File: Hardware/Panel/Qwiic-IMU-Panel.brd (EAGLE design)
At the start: 101.6 x 102.6 mm, 288 parts, among them J10 PTH, J11 SMD, J12 SPI, J17 SMD, J18 PTH, J19 SMD, J2 SMD, J20 SPI, J25 SMD, J26 PTH, J27 SMD, J28 SPI, J3 PTH, J33 SMD, J34 PTH, J35 SMD, J36 SPI, J4 SMD, J41 SMD, J42 PTH, J43 SMD, J44 SPI, J49 SMD, J50 PTH, J51 SMD, J52 SPI, J57 SMD, J58 PTH, J59 SMD, J6 SPI, J60 SPI, J65 SMD, J66 PTH, J67 SMD, J68 SPI, J9 SMD, U1 BNO080, U2 BNO080, U3 BNO080, U4 BNO080, U5 BNO080, U6 BNO080, U7 BNO080, U8 BNO080, U9 BNO080

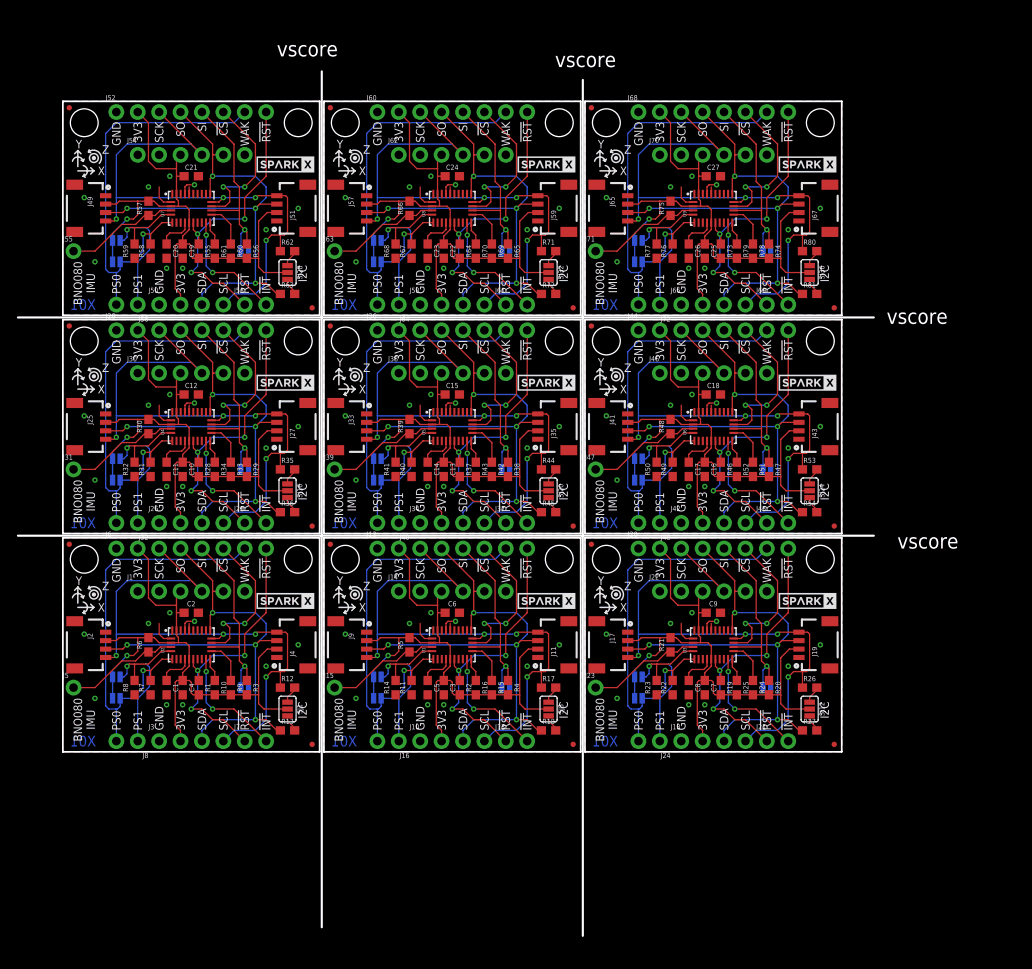
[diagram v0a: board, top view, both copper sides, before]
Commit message: Adding 32kHz xtal. Fixing UART silk.
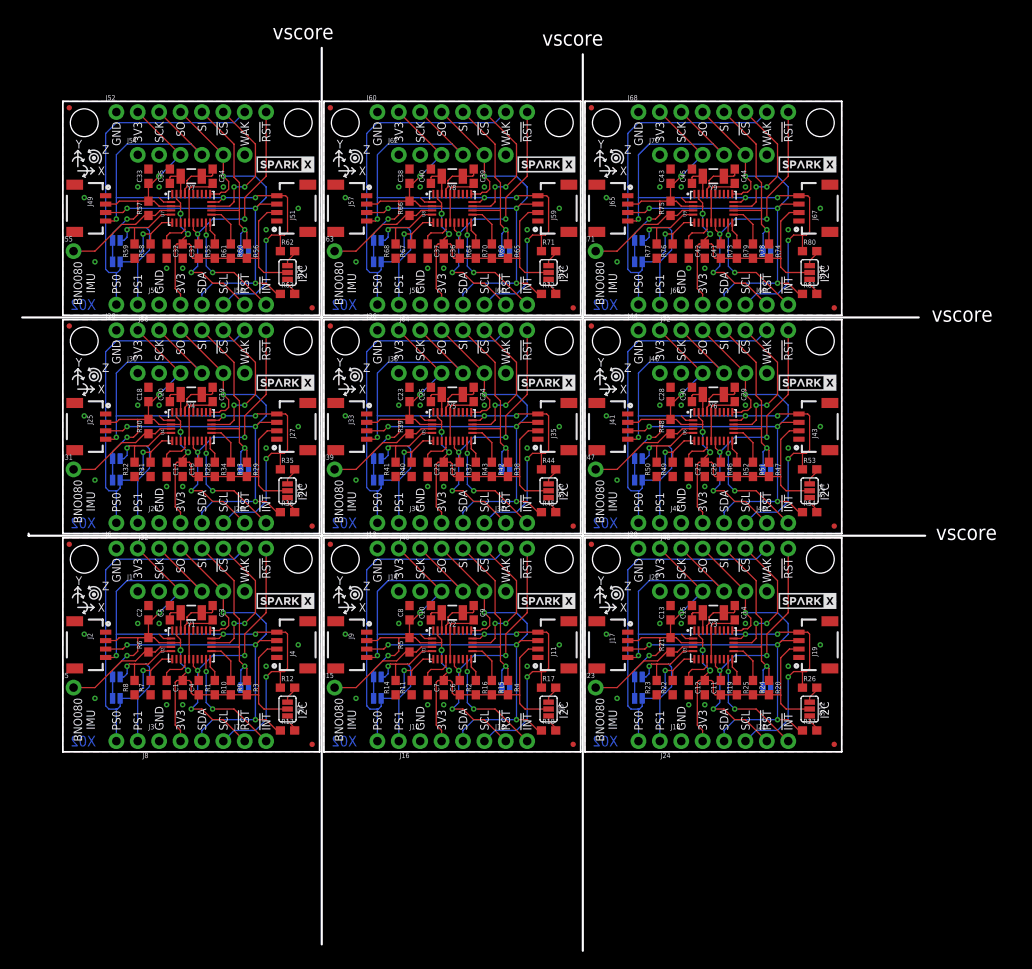
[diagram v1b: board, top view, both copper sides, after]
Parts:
- added C28, C31, C32, C33, C36, C37, C38, C41, C42, C43: 0.1uF, SparkFun-Capacitors:0603
- added C29, C30, C34, C35, C39, C40, C44, C45: 22pF, SparkFun-Capacitors:0603
- added Y1, Y2, Y3, Y4, Y5, Y6, Y7, Y8, Y9: 32.768kHz, SparkFun-Clocks:CRYSTAL-SMD-3.2X1.5MM
- C10, C14, C15, C19, C20, C24, C25, C3, C5, C9: value 0.1uF -> 22pF
- moved C11 68.9 mm to (76.2, 7.62)
- moved C12 68.5 mm to (74.3, 7.62), turned to 270 degrees
- moved C18 67.1 mm to (10.2, 42.4), turned to 90 degrees
- moved C16 62.0 mm to (14.2, 33.5)
- moved C17 62.0 mm to (12.3, 33.5)
- moved C21 45.9 mm to (45.2, 33.5), turned to 270 degrees
- moved C14 40.2 mm to (79.8, 16.5)
- moved C15 38.5 mm to (74.7, 16.5), turned to 90 degrees
- moved C25 36.7 mm to (43.7, 42.4), turned to 90 degrees
- moved C27 34.9 mm to (74.3, 33.5), turned to 270 degrees
- moved C8 34.3 mm to (41.1, 16.5), turned to 90 degrees
- moved C10 34.0 mm to (43.7, 16.5), turned to 90 degrees
- moved C7 32.9 mm to (43.3, 7.62)
- moved C5 31.9 mm to (12.7, 16.5), turned to 90 degrees
- moved C13 31.9 mm to (72.1, 16.5), turned to 90 degrees
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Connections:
- new net N$1: C5.1, U2.27, Y1.P$2
- new net N$10: C24.1, U5.26, Y5.P$1
- new net N$11: C30.1, U6.27, Y6.P$2
- new net N$12: C29.1, U6.26, Y6.P$1
- new net N$13: C35.1, U7.27, Y7.P$2
- new net N$14: C34.1, U7.26, Y7.P$1
- new net N$15: C40.1, U8.27, Y8.P$2
- new net N$16: C39.1, U8.26, Y8.P$1
- new net N$17: C45.1, U9.27, Y9.P$2
- new net N$18: C44.1, U9.26, Y9.P$1
- new net N$2: C3.1, U2.26, Y1.P$1
- new net N$3: C10.1, U1.27, Y2.P$2
- new net N$4: C9.1, U1.26, Y2.P$1
- new net N$5: C15.1, U3.27, Y3.P$2
- new net N$6: C14.1, U3.26, Y3.P$1
- new net N$7: C20.1, U4.27, Y4.P$2
- new net N$8: C19.1, U4.26, Y4.P$1
- new net N$9: C25.1, U5.27, Y5.P$2
- net 3.3V: no longer U2.10
- net 3.3V1: now also C8.1; no longer C3.1, U1.10
- net 3.3V2: now also C11.1, C13.1; no longer C7.1, C9.1, U3.10
- net 3.3V3: now also C16.1, C18.1; no longer C10.1, C12.1, U4.10
- net 3.3V4: now also C21.1, C23.1; no longer C13.1, C15.1, U5.10
- net 3.3V5: now also C26.1, C28.1; no longer C16.1, C18.1, U6.10
- net 3.3V6: now also C31.1, C33.1; no longer C19.1, C21.1, U7.10
- net 3.3V7: now also C36.1, C38.1; no longer C22.1, C24.1, U8.10
- net 3.3V8: now also C41.1, C43.1; no longer C25.1, C27.1, U9.10
- net CAP1: now also C7.1; no longer C5.1
- net CAP2: now also C12.1; no longer C8.1
- net CAP3: now also C17.1; no longer C11.1
- net CAP4: now also C22.1; no longer C14.1
- net CAP5: now also C27.1; no longer C17.1
- net CAP6: now also C32.1; no longer C20.1
- net CAP7: now also C37.1; no longer C23.1
- net CAP8: now also C42.1; no longer C26.1
- net GND: now also C3.2, C5.2, U2.10; no longer U2.26
- net GND1: now also C10.2, C7.2, C8.2, C9.2, U1.10; no longer C3.2, C5.2, U1.26
- net GND2: now also C11.2, C12.2, C13.2, C14.2, C15.2, U3.10; no longer C7.2, C8.2, C9.2, U3.26
- net GND3: now also C16.2, C17.2, C18.2, C19.2, C20.2, U4.10; no longer C10.2, C11.2, C12.2, U4.26
- net GND4: now also C21.2, C22.2, C23.2, C24.2, C25.2, U5.10; no longer C13.2, C14.2, C15.2, U5.26
- net GND5: now also C26.2, C27.2, C28.2, C29.2, C30.2, U6.10; no longer C16.2, C17.2, C18.2, U6.26
- net GND6: now also C31.2, C32.2, C33.2, C34.2, C35.2, U7.10; no longer C19.2, C20.2, C21.2, U7.26
- net GND7: now also C36.2, C37.2, C38.2, C39.2, C40.2, U8.10; no longer C22.2, C23.2, C24.2, U8.26
- net GND8: now also C41.2, C42.2, C43.2, C44.2, C45.2, U9.10; no longer C25.2, C26.2, C27.2, U9.26
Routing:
- net N$18: track 0.00 -> 5.74 mm
- net N$6: track 0.00 -> 5.74 mm
- net N$12: track 0.00 -> 5.74 mm
- net N$14: track 0.00 -> 5.74 mm
- net N$16: track 0.00 -> 5.74 mm
- net N$8: track 0.00 -> 5.74 mm
- net N$2: track 0.00 -> 5.74 mm
- net N$4: track 0.00 -> 5.74 mm
- net N$10: track 0.00 -> 5.74 mm
- net N$3: track 0.00 -> 4.18 mm
- net N$1: track 0.00 -> 4.18 mm
- net N$9: track 0.00 -> 4.18 mm
- net N$7: track 0.00 -> 4.18 mm
- net N$5: track 0.00 -> 4.18 mm
- net N$15: track 0.00 -> 4.18 mm
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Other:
- board size 101.6 x 102.6 mm -> 107.2 x 107.2 mm
- board text added: "X02"
- board text removed: "3V#"
- board text removed: "X01"
